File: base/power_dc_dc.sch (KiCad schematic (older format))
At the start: 0 parts

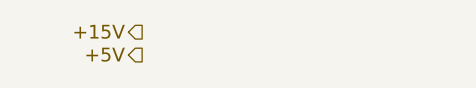
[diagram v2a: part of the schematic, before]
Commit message: draft 0.03 of mosfets_sens_isol.sch
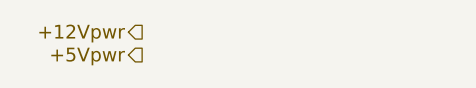
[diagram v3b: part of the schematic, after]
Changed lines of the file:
@@
 LIBS:ir
 LIBS:power
+LIBS:analog_devices
+LIBS:nxp
+LIBS:Logic_74xx
 LIBS:4hbd-base-cache
 EELAYER 25 0
@@
 +24VP
 Text HLabel 5000 2900 0    60   Output ~ 0
-+15V
++12Vpwr
 Text HLabel 5000 3000 0    60   Output ~ 0
-+5V
++5Vpwr
 Text HLabel 7300 3000 0    60   UnSpc ~ 0
 GNDP

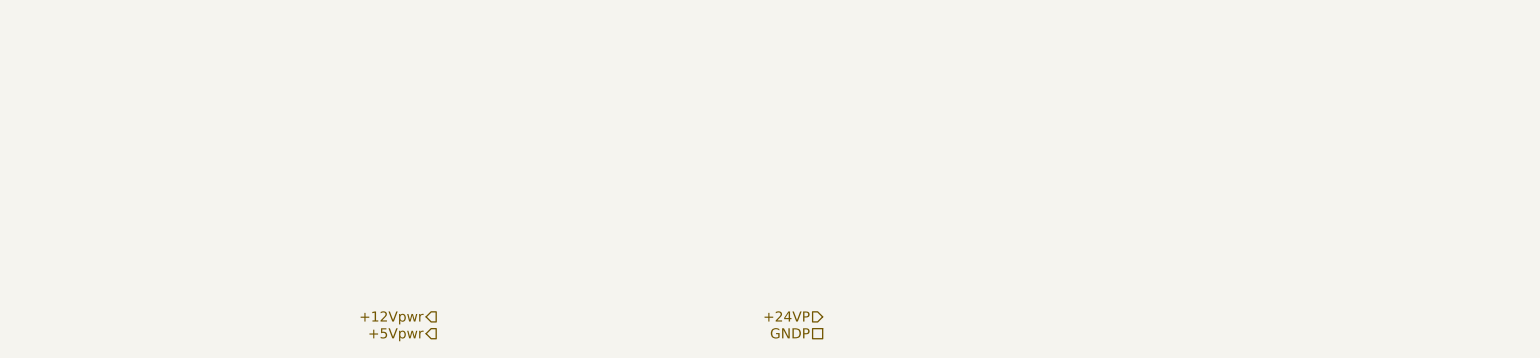
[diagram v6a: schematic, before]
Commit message: Update schematics: 1. Connect analog voltages to MCU board connector 2. Implement Power DC/DC
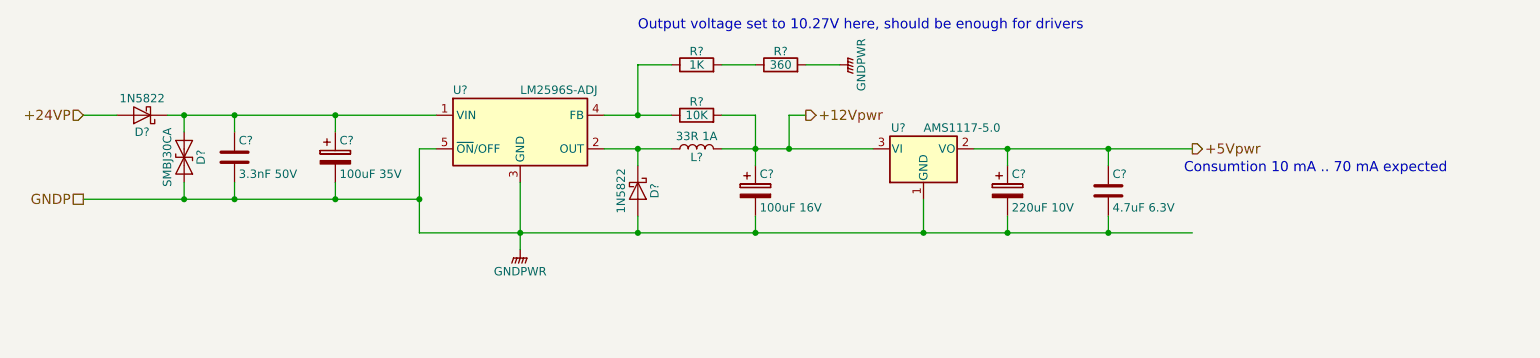
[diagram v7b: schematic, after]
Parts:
- added C?: 100uF 35V, Capacitor_SMD:CP_Elec_6.3x7.7, symbol CP
- added C?: 3.3nF 50V, Capacitor_SMD:C_0603_1608Metric, symbol C
- added C?: 100uF 16V, Capacitor_SMD:CP_Elec_6.3x5.3, symbol CP
- added C?: 220uF 10V, Capacitor_SMD:CP_Elec_6.3x5.3, symbol CP
- added C?: 4.7uF 6.3V, Capacitor_SMD:C_0603_1608Metric, symbol C
- added D? (x2): 1N5822, Diode_SMD:D_SMA, symbol 1N5822
- added D?: SMBJ30CA, Diode_SMD:D_SMB, symbol D_TVS
- added L?: 33R 1A, Inductor_SMD:L_7.3x7.3_H3.5, symbol L
- added R?: 10K, Resistor_SMD:R_0603_1608Metric, symbol R
- added R?: 1K, Resistor_SMD:R_0603_1608Metric, symbol R
- added R?: 360, Resistor_SMD:R_0603_1608Metric, symbol R
- added U?: AMS1117-5.0, Package_TO_SOT_SMD:SOT-223, symbol AP1117-15
- added U?: LM2596S-ADJ, TO_SOT_Packages_SMD:TO-263-5_TabPin3, symbol LM2596S-ADJ
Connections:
- net +12Vpwr: now also C?.1, L?.2, R?.2, U?.3 (VI)
- net +24VP: now also D?.2 (A)
- net +5Vpwr: now also C?.1, C?.1, U?.2 (VO)
- new net: C?.1, C?.1, D?.1 (A1), D?.1 (K), U?.1 (VIN)
- new net: D?.1 (K), L?.1, U?.2 (OUT)
- new net: R?.1, R?.1, U?.4 (FB)
- new net: R?.1, R?.2
- new net GNDPWR: C?.2, C?.2, C?.2, C?.2, C?.2, D?.2 (A), D?.2 (A2), R?.2, U?.1 (GND), U?.3 (GND), U?.5 (~ON~/OFF)
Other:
- note added: "Consumtion 10 mA .. 70 mA expected"
- note added: "Output voltage set to 10.27V here, should be enough for drivers"
